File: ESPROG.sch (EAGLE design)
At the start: 20 parts, among them IC1 CP2104, J1 USB-C, J2 M06RA, Q3 MMDT3904

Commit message: Renumbered parts
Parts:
- renumbered Q3 to Q1, R18 to R6
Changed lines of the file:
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@@
 <part name="U$5" library="SuperHouse-SupplySymbols" library_urn="urn:adsk.eagle:library:11790503" deviceset="5V" device=""/>
 <part name="J1" library="SuperHouse-Connectors" library_urn="urn:adsk.eagle:library:11765989" deviceset="USB-C" device="" package3d_urn="urn:adsk.eagle:package:7066538/2"/>
-<part name="R18" library="SuperHouse-DiscreteSemi" library_urn="urn:adsk.eagle:library:11768461" deviceset="RESISTOR" device="0603" package3d_urn="urn:adsk.eagle:package:11768543/2" value="5.1K"/>
+<part name="R6" library="SuperHouse-DiscreteSemi" library_urn="urn:adsk.eagle:library:11768461" deviceset="RESISTOR" device="0603" package3d_urn="urn:adsk.eagle:package:11768543/2" value="5.1K"/>
 <part name="IC1" library="SuperHouse-ICs" library_urn="urn:adsk.eagle:library:11768868" deviceset="CP2104" device="" package3d_urn="urn:adsk.eagle:package:7066298/2"/>
 <part name="GND1" library="SuperHouse-SupplySymbols" library_urn="urn:adsk.eagle:library:11790503" deviceset="GND" device=""/>
@@
 <part name="R4" library="SuperHouse-DiscreteSemi" library_urn="urn:adsk.eagle:library:11768461" deviceset="RESISTOR" device="0603" package3d_urn="urn:adsk.eagle:package:11768543/2" value="10K"/>
 <part name="R5" library="SuperHouse-DiscreteSemi" library_urn="urn:adsk.eagle:library:11768461" deviceset="RESISTOR" device="0603" package3d_urn="urn:adsk.eagle:package:11768543/2" value="10K"/>
-<part name="Q3" library="SuperHouse-DiscreteSemi" library_urn="urn:adsk.eagle:library:11768461" deviceset="TRANS_NPN_DUAL" device="-MMDT3904" package3d_urn="urn:adsk.eagle:package:11799616/2" value="MMDT3904"/>
+<part name="Q1" library="SuperHouse-DiscreteSemi" library_urn="urn:adsk.eagle:library:11768461" deviceset="TRANS_NPN_DUAL" device="-MMDT3904" package3d_urn="urn:adsk.eagle:package:11799616/2" value="MMDT3904"/>
 <part name="C2" library="SuperHouse-DiscreteSemi" library_urn="urn:adsk.eagle:library:11768461" deviceset="CAP" device="0603" package3d_urn="urn:adsk.eagle:package:7066315/6" value="1uF"/>
 <part name="GND7" library="SuperHouse-SupplySymbols" library_urn="urn:adsk.eagle:library:11790503" deviceset="GND" device=""/>
@@
 <attribute name="VALUE" x="30.48" y="116.84" size="1.778" layer="96"/>
 </instance>
-<instance part="R18" gate="G$1" x="12.7" y="93.98" smashed="yes" rot="R90">
+<instance part="R6" gate="G$1" x="12.7" y="93.98" smashed="yes" rot="R90">
 <attribute name="NAME" x="11.2014" y="90.17" size="1.778" layer="95" rot="R90"/>
 <attribute name="VALUE" x="16.002" y="90.17" size="1.778" layer="96" rot="R90"/>
@@
 <attribute name="VALUE" x="182.88" y="90.678" size="1.778" layer="96"/>
 </instance>
-<instance part="Q3" gate="Q1" x="193.04" y="111.76" smashed="yes">
+<instance part="Q1" gate="Q1" x="193.04" y="111.76" smashed="yes">
 <attribute name="NAME" x="189.23" y="115.57" size="1.778" layer="95" font="vector"/>
 <attribute name="VALUE" x="187.96" y="106.934" size="1.778" layer="96" font="vector"/>
 </instance>
-<instance part="Q3" gate="Q2" x="193.04" y="93.98" smashed="yes" rot="MR180">
+<instance part="Q1" gate="Q2" x="193.04" y="93.98" smashed="yes" rot="MR180">
 <attribute name="NAME" x="189.23" y="97.79" size="1.778" layer="95" font="vector"/>
 <attribute name="VALUE" x="187.96" y="89.154" size="1.778" layer="96" font="vector"/>
@@
 <junction x="27.94" y="88.9"/>
 <wire x1="27.94" y1="88.9" x2="17.78" y2="88.9" width="0.1524" layer="91"/>
-<pinref part="R18" gate="G$1" pin="1"/>
+<pinref part="R6" gate="G$1" pin="1"/>
 <wire x1="12.7" y1="88.9" x2="17.78" y2="88.9" width="0.1524" layer="91"/>
 <junction x="17.78" y="88.9"/>
@@
 <wire x1="12.7" y1="99.06" x2="38.1" y2="99.06" width="0.1524" layer="91"/>
 <wire x1="38.1" y1="99.06" x2="38.1" y2="101.6" width="0.1524" layer="91"/>
-<pinref part="R18" gate="G$1" pin="2"/>
+<pinref part="R6" gate="G$1" pin="2"/>
 <junction x="12.7" y="99.06"/>
 </segment>
@@
 <net name="EN" class="0">
 <segment>
-<pinref part="Q3" gate="Q1" pin="C"/>
+<pinref part="Q1" gate="Q1" pin="C"/>
 <wire x1="195.58" y1="116.84" x2="195.58" y2="119.38" width="0.1524" layer="91"/>
 <pinref part="J2" gate="G$1" pin="2"/>
@@
 <net name="GPIO0" class="0">
 <segment>
-<pinref part="Q3" gate="Q2" pin="C"/>
+<pinref part="Q1" gate="Q2" pin="C"/>
 <wire x1="195.58" y1="88.9" x2="195.58" y2="86.36" width="0.1524" layer="91"/>
 <wire x1="195.58" y1="86.36" x2="203.2" y2="86.36" width="0.1524" layer="91"/>
@@
 <net name="N$7" class="0">
 <segment>
-<pinref part="Q3" gate="Q1" pin="B"/>
+<pinref part="Q1" gate="Q1" pin="B"/>
 <pinref part="R4" gate="G$1" pin="2"/>
 </segment>
@@
 <net name="N$8" class="0">
 <segment>
-<pinref part="Q3" gate="Q2" pin="B"/>
+<pinref part="Q1" gate="Q2" pin="B"/>
 <pinref part="R5" gate="G$1" pin="2"/>
 </segment>
@@
 <wire x1="177.8" y1="104.14" x2="180.34" y2="101.6" width="0.1524" layer="91"/>
 <wire x1="180.34" y1="101.6" x2="195.58" y2="101.6" width="0.1524" layer="91"/>
-<pinref part="Q3" gate="Q2" pin="E"/>
+<pinref part="Q1" gate="Q2" pin="E"/>
 <wire x1="195.58" y1="101.6" x2="195.58" y2="99.06" width="0.1524" layer="91"/>
 <wire x1="177.8" y1="111.76" x2="177.8" y2="134.62" width="0.1524" layer="91"/>
@@
 <wire x1="177.8" y1="101.6" x2="180.34" y2="104.14" width="0.1524" layer="91"/>
 <wire x1="180.34" y1="104.14" x2="195.58" y2="104.14" width="0.1524" layer="91"/>
-<pinref part="Q3" gate="Q1" pin="E"/>
+<pinref part="Q1" gate="Q1" pin="E"/>
 <wire x1="195.58" y1="104.14" x2="195.58" y2="106.68" width="0.1524" layer="91"/>
 <wire x1="177.8" y1="93.98" x2="175.26" y2="93.98" width="0.1524" layer="91"/>

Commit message: Replaced CP2104 with CP2102N for v1.1 release
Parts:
- removed C1: 4.7uF, SuperHouse-DiscreteSemi:CAP0603
- added R7: 22.1K, SuperHouse-DiscreteSemi:RESISTOR0603
- added R8: 47.5K, SuperHouse-DiscreteSemi:RESISTOR0603
- C2: value 1uF -> 4.7uF
- IC1: value CP2104 -> CP2102N-A01-GQFN24
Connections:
- net 3.3V: now also LED3.A; no longer R3.2
- net 5V: now also R7.2; no longer IC1.VBUS
- net GND: now also R3.1, R8.1; no longer C1.2, LED3.C
- net N$5: now also LED3.C, R3.2; no longer LED3.A, R3.1
- net N$6: now also IC1.VBUS, R7.1, R8.2; no longer C1.1, IC1.VPP
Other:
- note added: "V1.1 (2019-07-04)"
- note removed: "V1.0 (2019-06-21)"
- moved on the sheet: LED1, LED2, LED3, R1, R2, R3

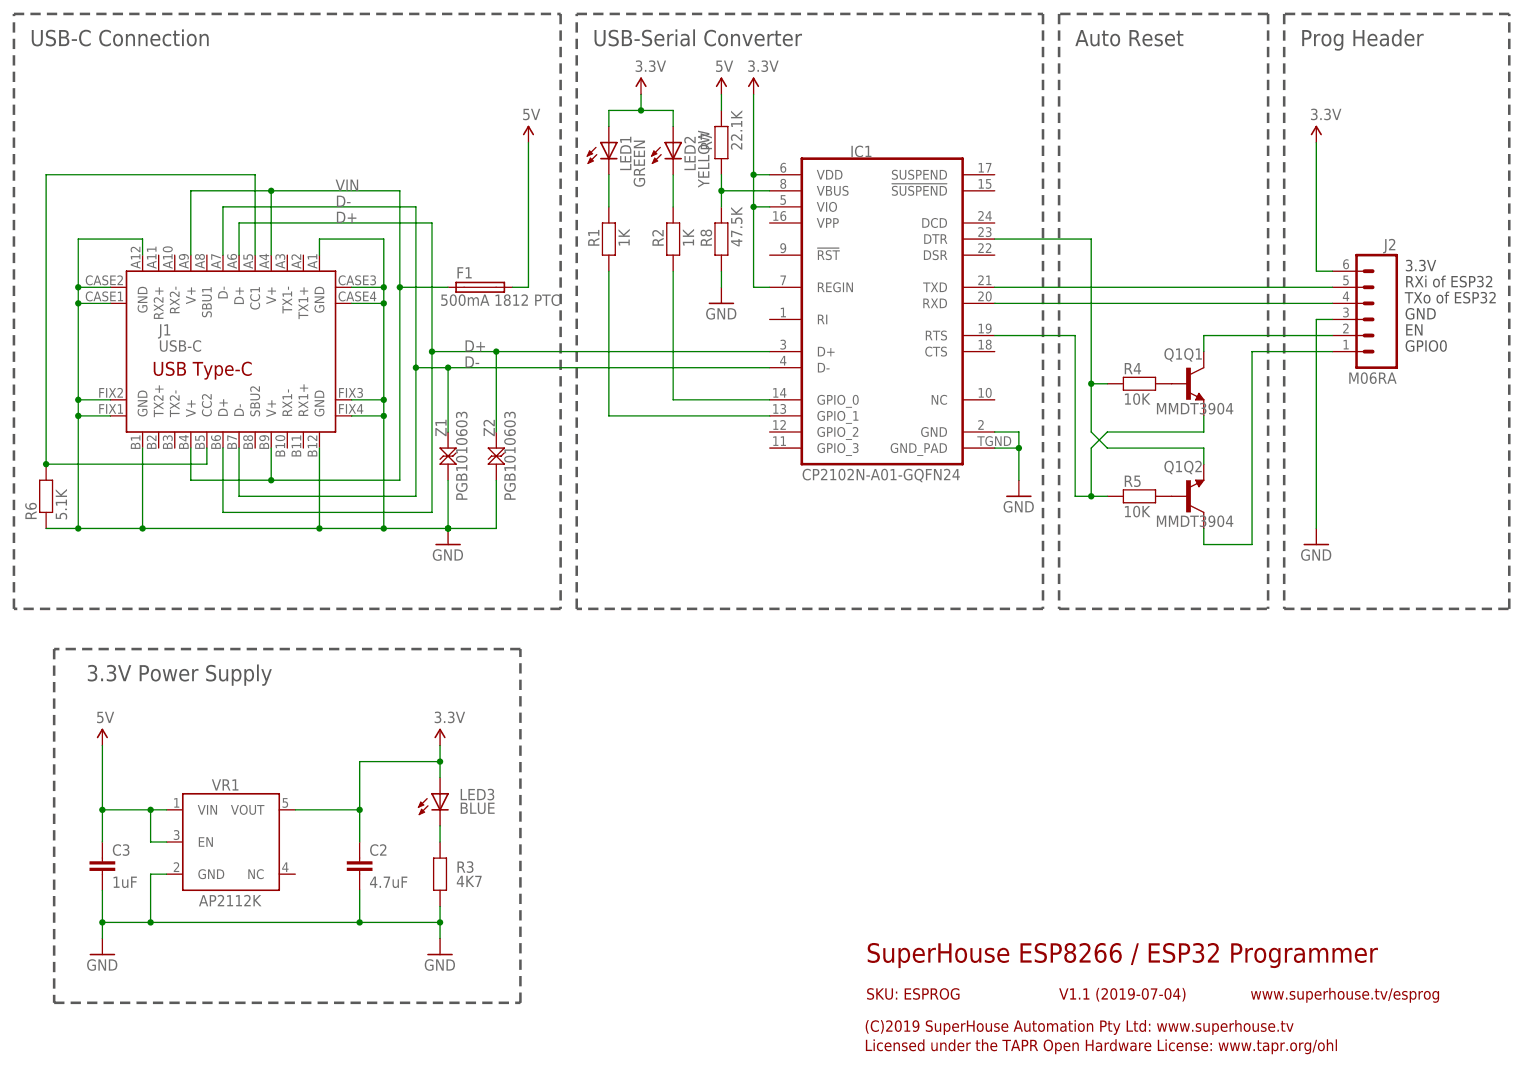
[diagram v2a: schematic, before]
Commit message: Split CC1 and CC2 on USB connector
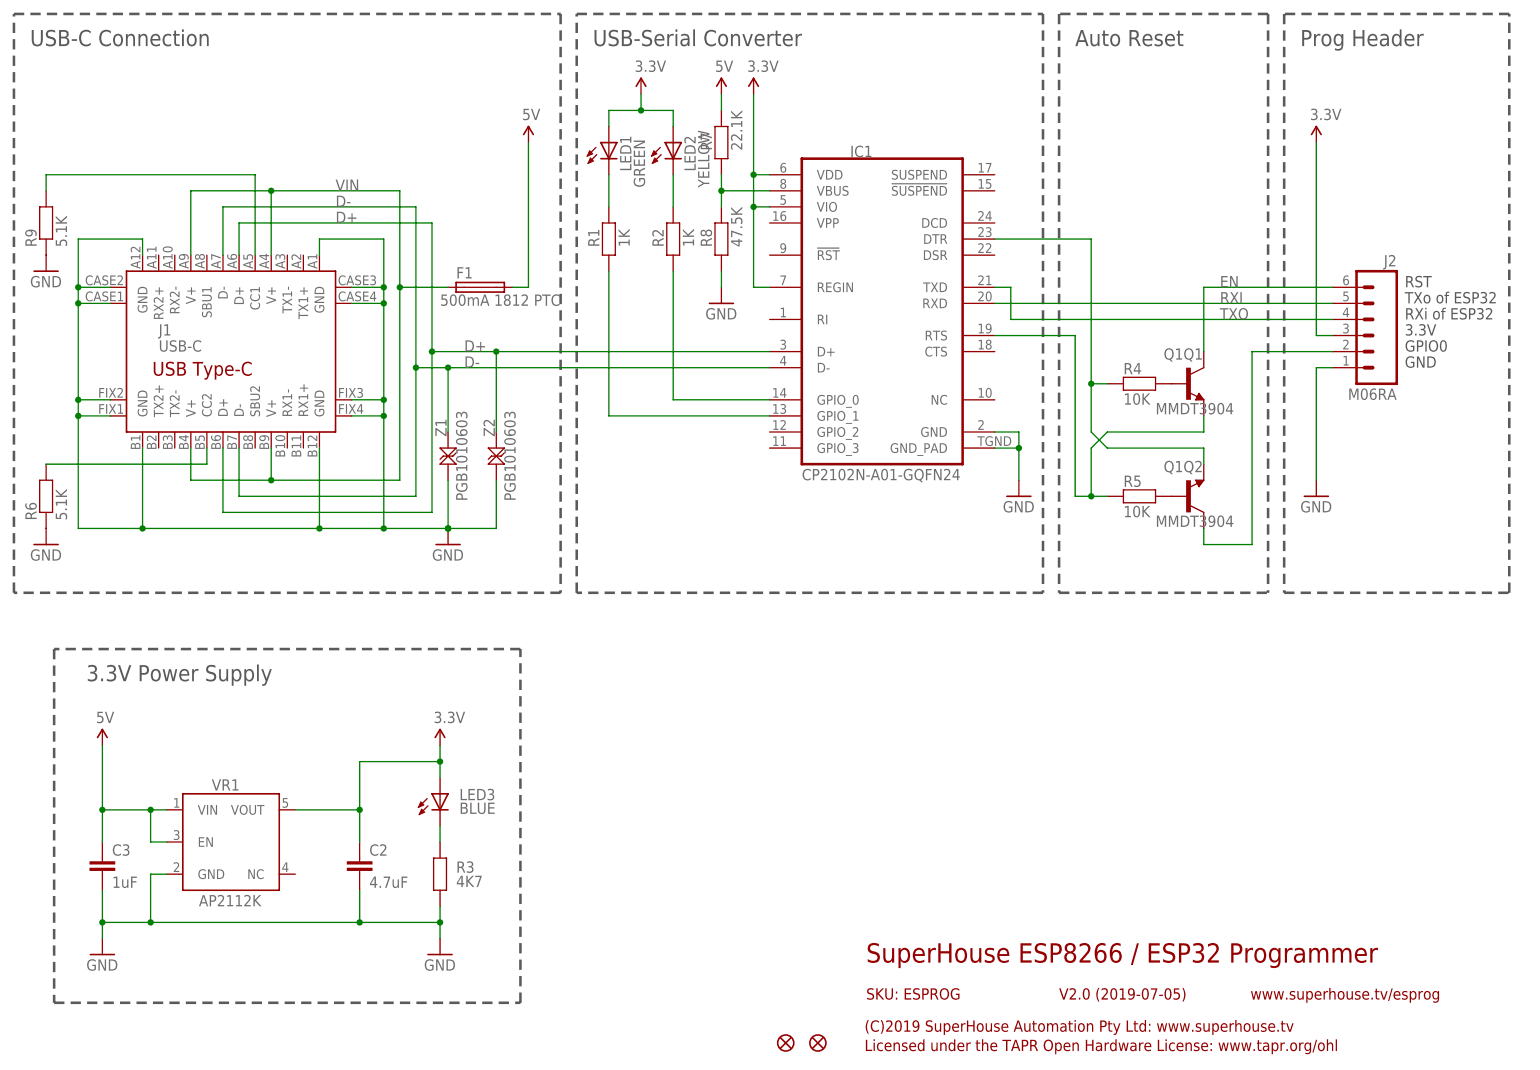
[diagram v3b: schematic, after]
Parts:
- added FID1, FID2: FIDUCIAL1X2.5, freetronics:FIDUCIAL1X2.5
- added R9: 5.1K, SuperHouse-DiscreteSemi:RESISTOR0603
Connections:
- removed net N$10: IC1.RXD, J2.4
- new net RXI: IC1.RXD, J2.5
- new net TXO: IC1.TXD, J2.4
- net 3.3V: now also J2.3; no longer J2.6
- net EN: now also J2.6; no longer J2.2
- net GND: now also J2.1, R9.1; no longer J2.3
- net GPIO0: now also J2.2; no longer J2.1
- net N$67: now also R9.2; no longer J1.CC2, R6.2
- net N$9: now also J1.CC2, R6.2; no longer IC1.TXD, J2.5
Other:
- note added: "RST"
- note added: "V2.0 (2019-07-05)"
- note removed: "EN"
- note removed: "V1.1 (2019-07-04)"
- moved on the sheet: J2

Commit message: Major revision of header pinout
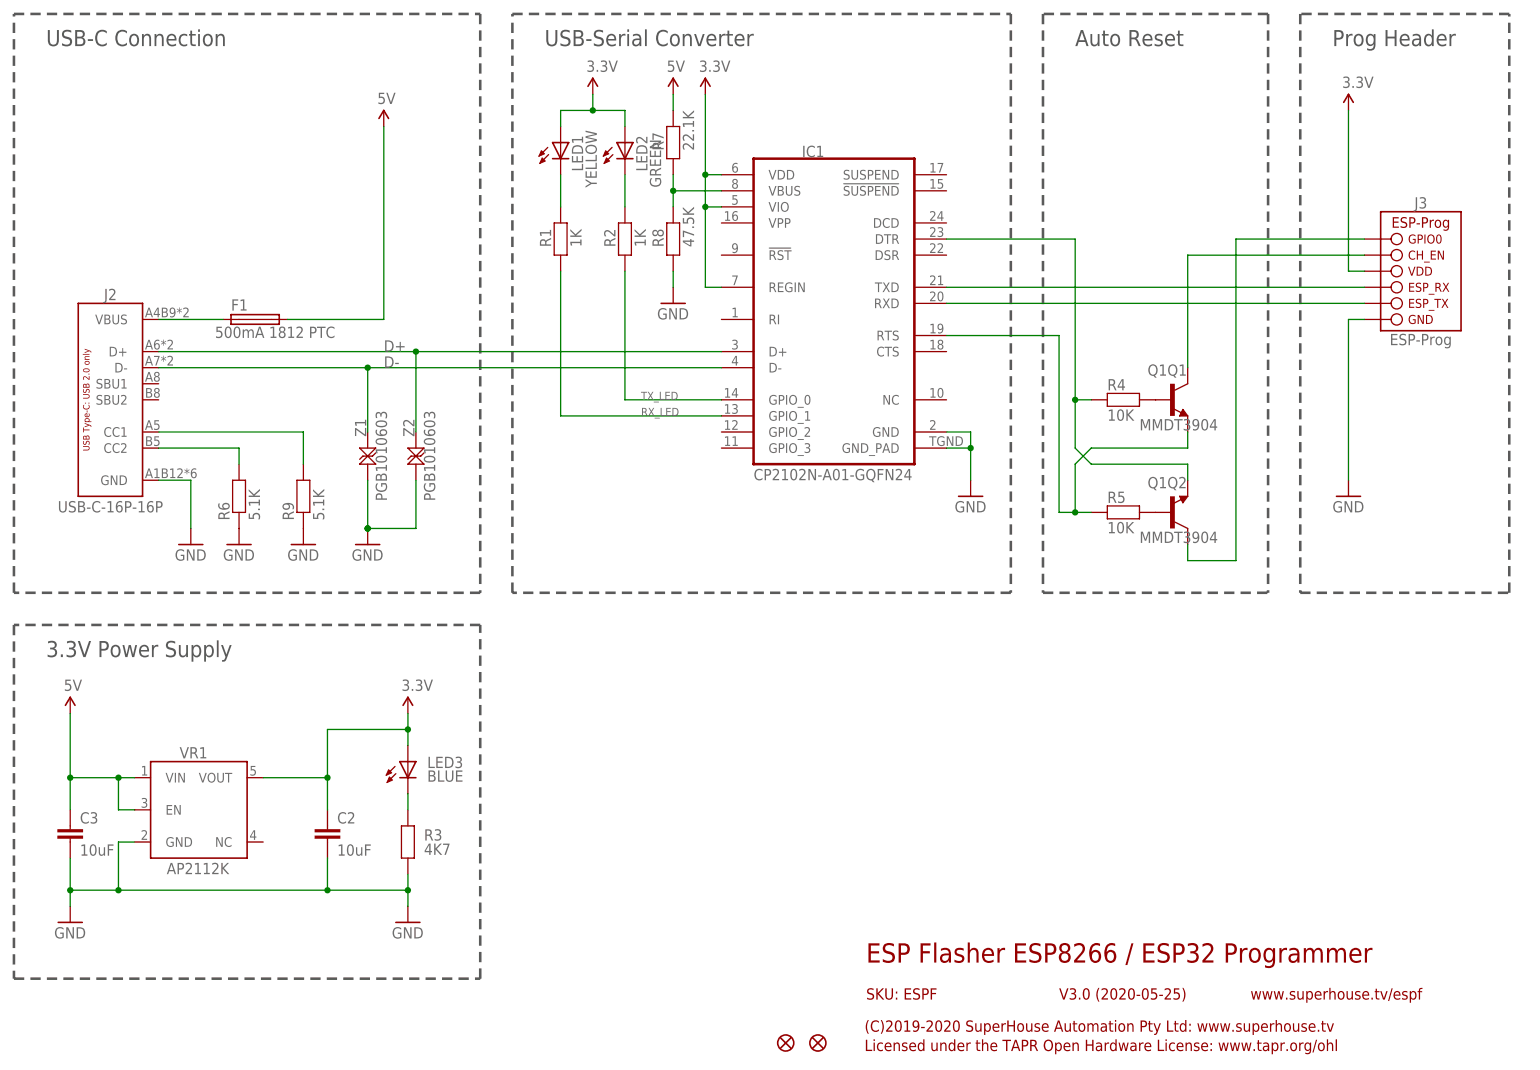
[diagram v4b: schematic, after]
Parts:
- removed J1: USB-C, SuperHouse-Connectors:USB-C
- added J3: ESP-PROG-1X6-2.54-PINS-RA, SuperHouse-ESP-Prog:ESP-PROG-1X6-2.54-PINS-RA
- C2: value 4.7uF -> 10uF; device SuperHouse-DiscreteSemi:CAP0603 -> SuperHouse-DiscreteSemi:CAP0805
- C3: value 1uF -> 10uF; device SuperHouse-DiscreteSemi:CAP0603 -> SuperHouse-DiscreteSemi:CAP0805
- J2: value M06RA -> USB-C-16P-16P; device SuperHouse-Connectors:M06RA -> SuperHouse-Connectors:USB-C-16P-16P
- LED1: value GREEN -> YELLOW
- LED2: value YELLOW -> GREEN
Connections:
- net N$1 renamed TX_LED
- net N$2 renamed RX_LED
- removed net N$67: J1.CC1, R9.2
- new net N$10: J2.CC1, R9.2
- net 3.3V: now also J3.VDD; no longer J2.3
- net D+: now also J2.D+; no longer J1.D+@A6, J1.D+@B6
- net D-: now also J2.D-; no longer J1.D-@A7, J1.D-@B7
- net EN: now also J3.CH_EN; no longer J2.6
- net GND: now also J2.GND, J3.GND; no longer J1.GND@A1, J1.GND@A12, J1.GND@B1, J1.GND@B12, J1.GND@CASE1, J1.GND@CASE2, J1.GND@CASE3, J1.GND@CASE4, J1.GND@FIX1, J1.GND@FIX2, J1.GND@FIX3, J1.GND@FIX4, J2.1
- net GPIO0: now also J3.GPIO0; no longer J2.2
- net N$9: now also J2.CC2; no longer J1.CC2
- net RXI: now also J3.ESP_TX; no longer J2.5
- net TXO: now also J3.ESP_RX; no longer J2.4
- net VIN: now also J2.VBUS; no longer J1.V+@A4, J1.V+@A9, J1.V+@B4, J1.V+@B9
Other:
- note added: "(C)2019-2020 SuperHouse Automation Pty Ltd: www.superhouse.tv"
- note added: "ESP Flasher ESP8266 / ESP32 Programmer"
- note added: "SKU: ESPF"
- note added: "V3.0 (2020-05-25)"
- note added: "www.superhouse.tv/espf"
- note removed: "(C)2019 SuperHouse Automation Pty Ltd: www.superhouse.tv"
- note removed: "3.3V"
- note removed: "GND"
- note removed: "GPIO0"
- note removed: "RST"
- note removed: "RXi of ESP32"
- note removed: "SKU: ESPROG"
- note removed: "SuperHouse ESP8266 / ESP32 Programmer"
- note removed: "TXo of ESP32"
- note removed: "V2.0 (2019-07-05)"
- note removed: "www.superhouse.tv/esprog"
- moved on the sheet: C2, C3, F1, IC1, LED1, LED2, LED3, Q1Q1, Q1Q2, R1, R2, R3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
